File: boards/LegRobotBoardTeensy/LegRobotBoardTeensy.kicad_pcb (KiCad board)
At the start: 2 copper layers, 142.8 x 110.9 mm, 179 parts, among them J1 IDC, J10 IDC, J11 IDC, J12 IDC, J13 IDC, J14 IDC, J15 IDC, J16 IDC, J17 Conn_01x05, J18 Conn_01x05, J19 Conn_01x05, J2 B3B-XH-A, J20 Conn_01x05, J21 Conn_01x05, J22 Conn_01x05, J23 Conn_01x05, J24 Conn_01x05, J3 B3B-XH-A, J4 B3B-XH-A, J5 B3B-XH-A, J6 IDC, J7 IDC, J8 IDC, J9 IDC, Q1 AO3400A, Q10 AO3400A, Q11 AO3400A, Q12 AO3400A, Q13 AO3400A, Q14 AO3400A, Q15 AO3400A, Q16 AO3400A, Q17 AO3400A, Q18 AO3400A, Q19 AO3400A, Q2 AO3400A, Q20 AO3400A, Q21 AO3400A, Q22 AO3400A, Q23 AO3400A, Q24 AO3400A, Q3 AO3400A, Q4 AO3400A, Q5 AO3400A, Q6 AO3400A, Q7 AO3400A, Q8 AO3400A, Q9 AO3400A, U1 Teensy4.0, U11 IS31FL3739-GRLS4-TR, U2 TLC555CDR, U3 SN74HC08DR, U4 SN74HC08DR, U5 PCA9685PW_118, U6 SN74HC08DR, U7 SN74HC08DR, U8 BNO055

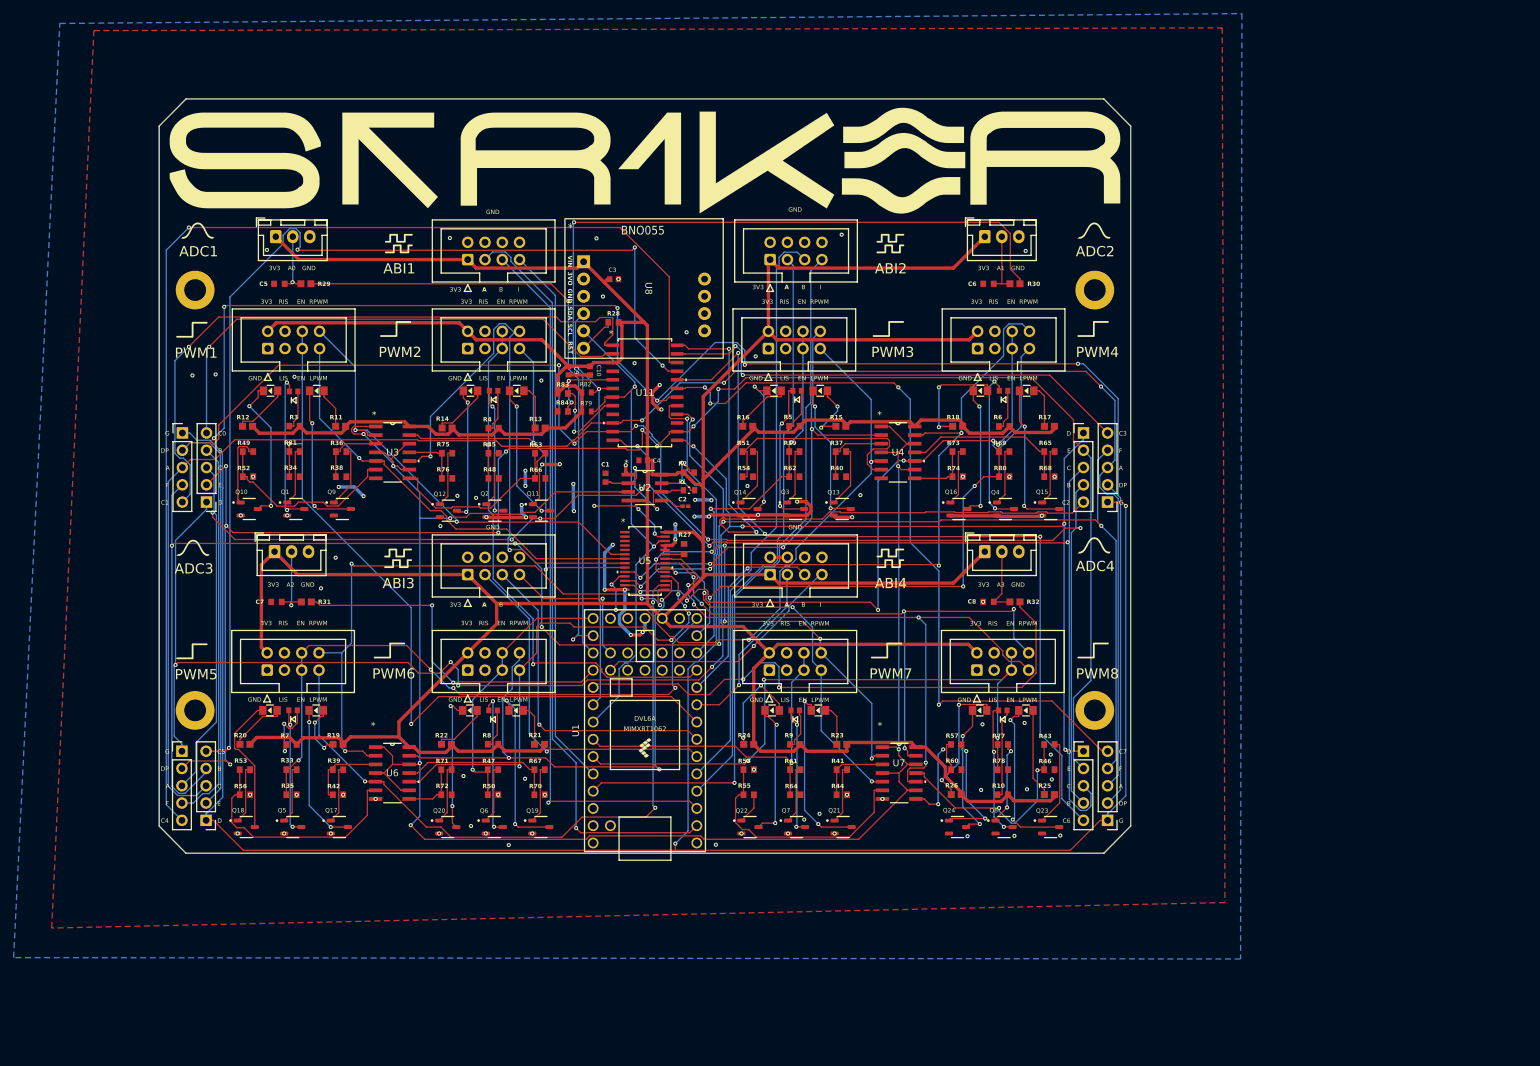
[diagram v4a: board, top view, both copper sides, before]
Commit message: Leg board re-do LED displays, main board prepare for re-routing
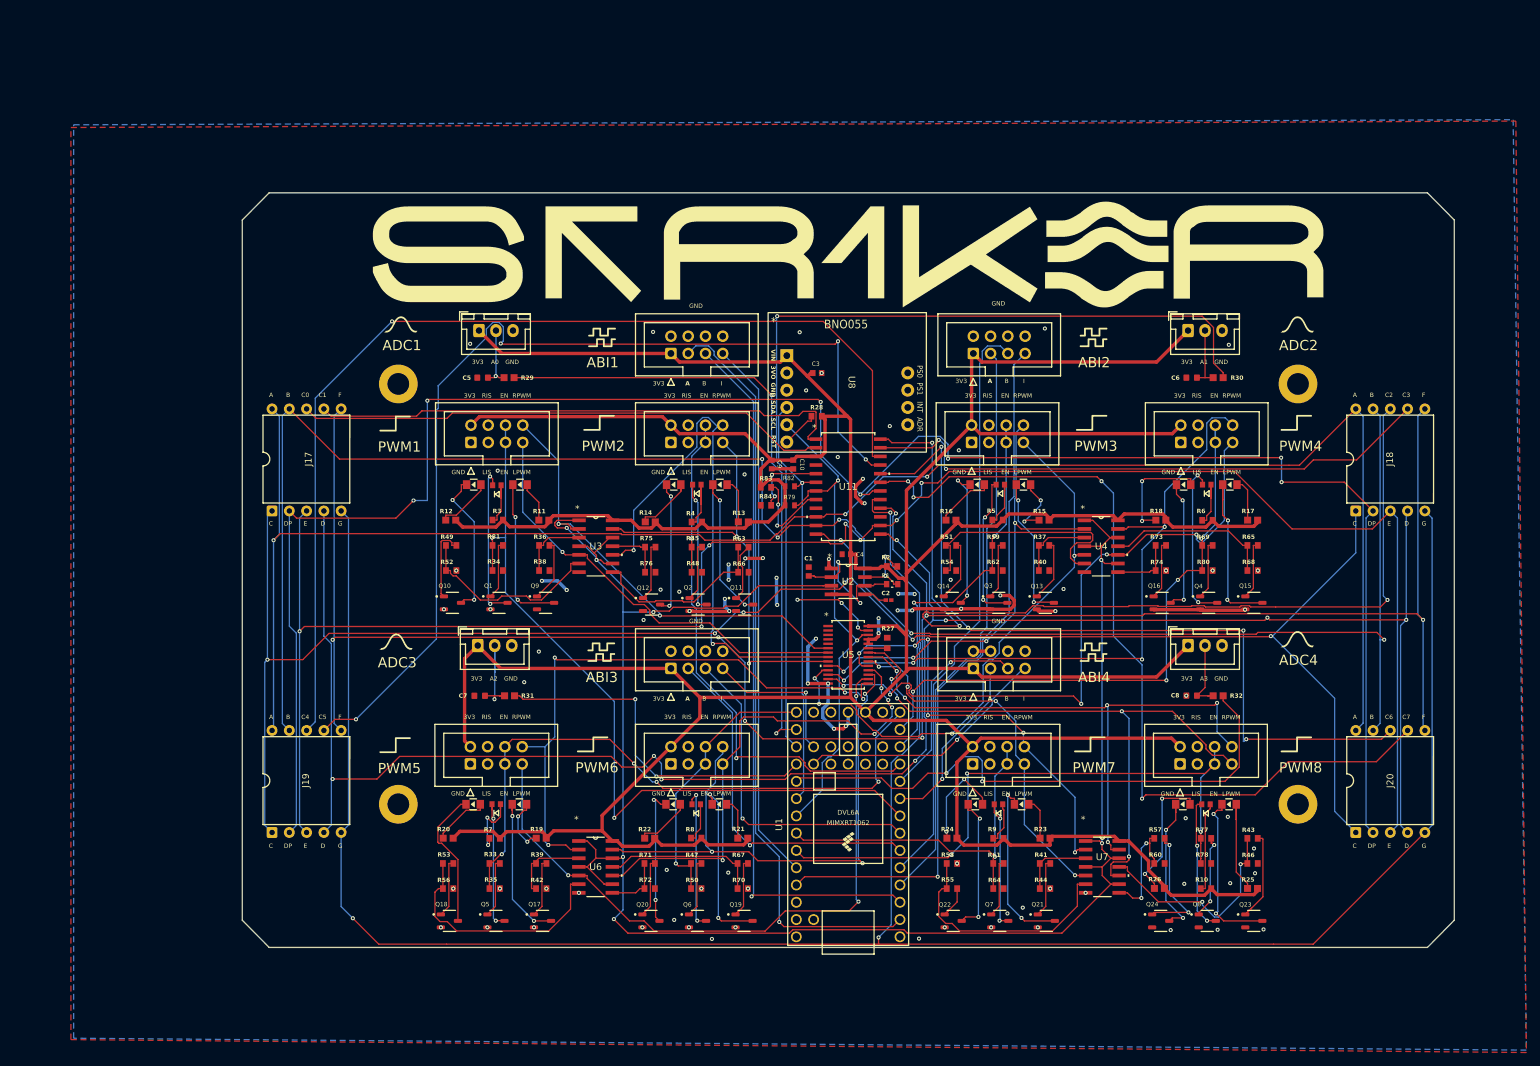
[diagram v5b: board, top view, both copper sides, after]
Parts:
- removed J21, J22, J23, J24: Conn_01x05, Connector_PinHeader_2.54mm:PinHeader_1x05_P2.54mm_Vertical
- J17, J18, J19, J20: value Conn_01x05 -> Conn_01x10; footprint Connector_PinHeader_2.54mm:PinHeader_1x05_P2.54mm_Vertical -> DIP:DIP-10_W15.24mm
- moved J18 169.0 mm to (228.5, 80.5), turned to 90 degrees
- moved J19 133.0 mm to (69.2, 127.8), turned to 90 degrees
- moved J20 60.8 mm to (228.5, 127.8), turned to 90 degrees
- moved C9 32.9 mm to (142.7, 73.7)
- moved R79 32.9 mm to (145.3, 79.7)
- moved R82 32.9 mm to (145.3, 76.9)
- moved U8 32.9 mm to (153.9, 61.6)
- moved C1 32.9 mm to (148.1, 89.4)
- moved C2 32.9 mm to (159.8, 93.6)
- moved C3 32.9 mm to (149.4, 60.2)
- moved C4 32.9 mm to (153.6, 86.9)
- moved C5 32.9 mm to (100.2, 60.9)
- moved C6 32.9 mm to (204.4, 60.9)
- moved C7 32.9 mm to (99.7, 107.7)
- moved C8 32.9 mm to (204.4, 107.7)
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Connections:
- J17 pad 1: DIGIT_G -> DIGIT_C
- J17 pad 3: DIGIT_A -> DIGIT_E
- J17 pad 4: DIGIT_F -> DIGIT_D
- J17 pad 5: COM1 -> DIGIT_G
- J18 pad 1: DIGIT_D -> DIGIT_C
- J18 pad 2: DIGIT_E -> DIGIT_DP
- J18 pad 3: DIGIT_C -> DIGIT_E
- J18 pad 4: DIGIT_B -> DIGIT_D
- J18 pad 5: COM0 -> DIGIT_G
- J19 pad 1: DIGIT_D -> DIGIT_C
- J19 pad 2: DIGIT_E -> DIGIT_DP
- J19 pad 3: DIGIT_C -> DIGIT_E
- J19 pad 4: DIGIT_B -> DIGIT_D
- J19 pad 5: COM2 -> DIGIT_G
- J20 pad 1: DIGIT_G -> DIGIT_C
- J20 pad 3: DIGIT_A -> DIGIT_E
- J20 pad 4: DIGIT_F -> DIGIT_D
- J20 pad 5: COM3 -> DIGIT_G
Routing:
- net COM2: track 98.0 -> 141.3 mm, vias 2 -> 3
- net DIGIT_D: track 262.1 -> 297.5 mm
- net DIGIT_G: track 322.4 -> 349.3 mm
- net COM4: track 176.9 -> 152.7 mm
- net DIGIT_E: track 258.3 -> 282.3 mm, vias 9 -> 7
- net DIGIT_B: track 263.3 -> 283.9 mm
- net DIGIT_C: track 252.8 -> 272.9 mm
- net DIGIT_F: track 287.4 -> 306.3 mm
- net COM1: track 95.7 -> 79.3 mm, vias 1 -> 0
- net COM7: track 113.2 -> 128.3 mm
- net COM3: track 71.2 -> 85.6 mm
- net COM5: track 159.4 -> 147.9 mm
- net COM6: track 123.8 -> 118.1 mm, vias 3 -> 4
- net Net-(J4-Pin_2): track 11.3 -> 16.0 mm
- net DIGIT_A: track 259.9 -> 264.3 mm
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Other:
- board size 142.8 x 110.9 mm -> 178.2 x 110.9 mm

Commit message: Re-export updated boards
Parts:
- moved MH2 27.5 mm to (236.8, 40.0)
- moved MH1 27.5 mm to (71.0, 40.0)
- moved MH4 22.3 mm to (236.8, 138.3)
- moved MH3 22.3 mm to (71.0, 138.3)
